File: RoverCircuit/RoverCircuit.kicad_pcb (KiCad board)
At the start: 2 copper layers, 92.2 x 67.7 mm, 57 parts, among them J11_Sample_IR_Diode1 JST_2Pin_P2.54_V, J12_Sat_Diode1 JST_2Pin_P2.54_V, J13_Laser1 JST_2Pin_P2.54_V, J14_QRD_Board1 JST_5Pin_P2.54_V, J15_Ball_QRD1 JST_3Pin_P2.54_V, J1_Servo1 JST_3Pin_P2.54_V, J2_Left_Wheel1 JST_4Pin_P2.54_V, J3_Right_Wheel1 JST_4Pin_P2.54_V, J4 JST_10Pin_P2.54_V, J5 JST_10Pin_P2.54_V, J6_Left_Sharp1 JST_3Pin_P2.54_V, J7_Right_Sharp1 JST_3Pin_P2.54_V, J8_Front_Sharp1 JST_3Pin_P2.54_V, J9_5v_Regulator1 JST_3Pin_P2.54_V, Q1 PMOS, Q2 NMOS, Q6 NMOS, U2 LM1117T-3.3, U3 LM324

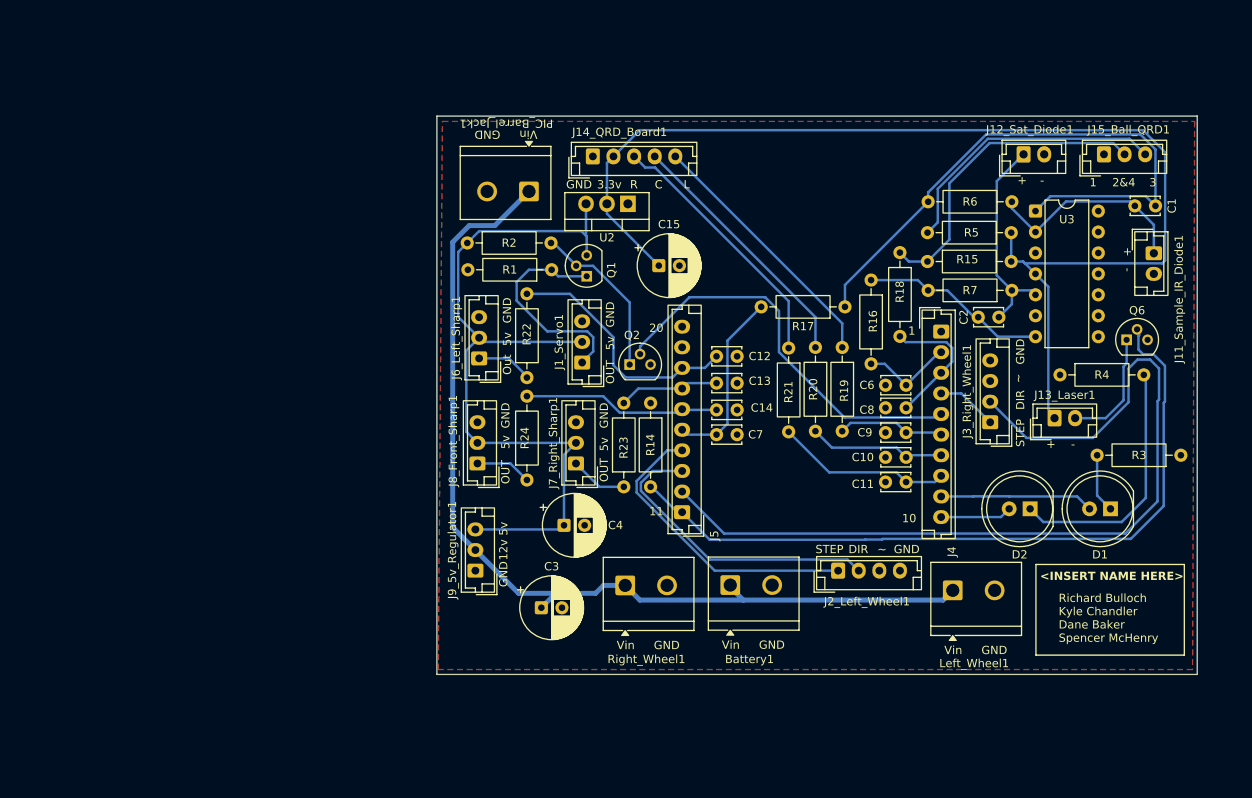
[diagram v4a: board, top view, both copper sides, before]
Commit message: Finalized circuit diagram, functional line following
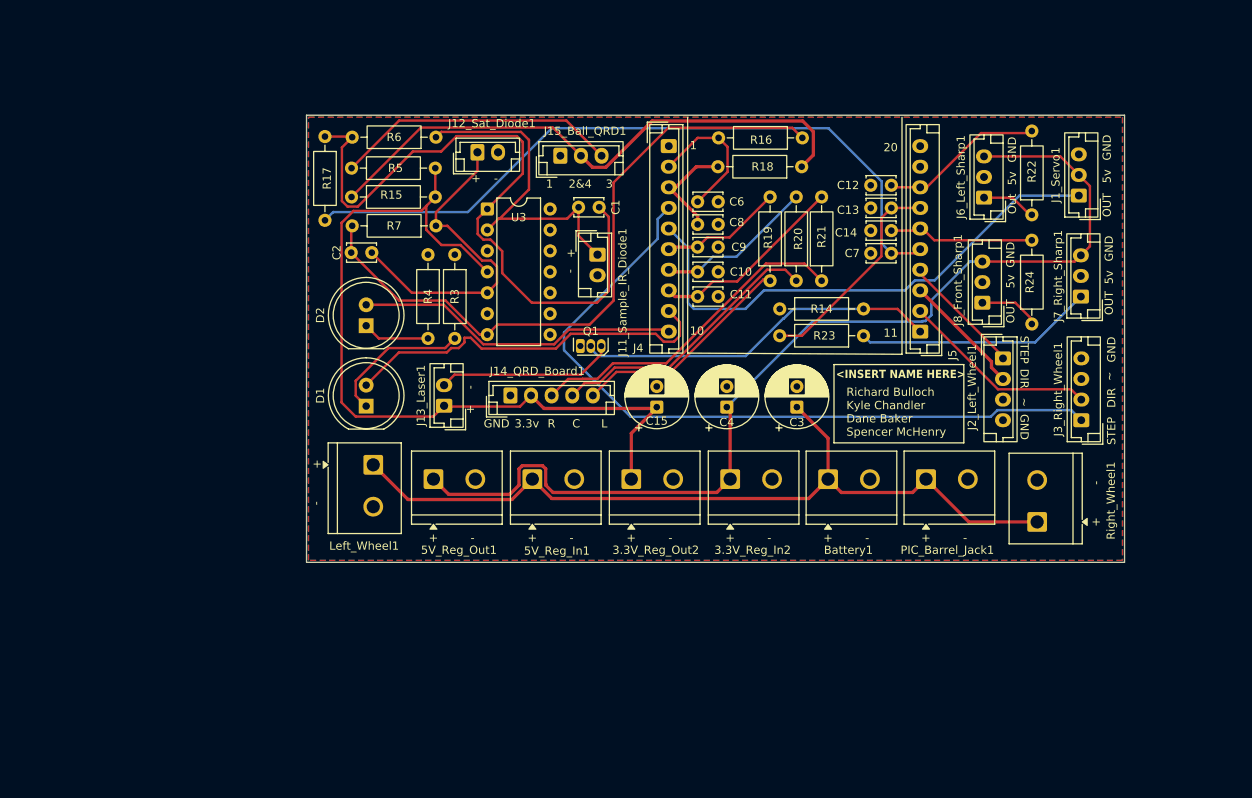
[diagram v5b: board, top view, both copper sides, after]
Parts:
- removed J9_5v_Regulator1: JST_3Pin_P2.54_V, Connector_JST:JST_EH_B3B-EH-A_1x03_P2.50mm_Vertical
- removed the Q1 at (120.5, 65.8)
- removed Q2: NMOS, Package_TO_SOT_THT:TO-92
- removed R1, R2: 10K, Resistor_THT:R_Axial_DIN0207_L6.3mm_D2.5mm_P10.16mm_Horizontal
- removed U2: LM1117T-3.3, Package_TO_SOT_THT:TO-220-3_Vertical
- added 3.3V_Reg_In2: Battery_Terminal, Custom_Library:screw_terminal, F.Cu at (140.6, 90.7)
- added 3.3V_Reg_Out2: Battery_Terminal, Custom_Library:screw_terminal, F.Cu at (128.6, 90.7)
- added 5V_Reg_In1: Battery_Terminal, Custom_Library:screw_terminal, F.Cu at (116.6, 90.7)
- added 5V_Reg_Out1: Battery_Terminal, Custom_Library:screw_terminal, F.Cu at (104.6, 90.7)
- Q1: renamed from Q6; value NMOS -> VN2106; footprint Package_TO_SOT_THT:TO-92 -> Package_TO_SOT_THT:TO-92S
- R16, R17, R18, R19, R20, R21, R22, R23, R24: value 150Ω -> 10kΩ
- R3, R4: value 330 -> 330Ω
- moved R3 91.4 mm to (104.5, 63.2), turned to -90 degrees
- moved D1 91.1 mm to (93.8, 81.5), turned to 90 degrees
- moved D2 83.5 mm to (93.8, 71.8), turned to 90 degrees
- moved R4 78.0 mm to (101.2, 63.2), turned to -90 degrees
- moved C2 76.5 mm to (94.4, 62.9)
- moved Left_Wheel1 74.5 mm to (94.3, 91.4), turned to -90 degrees
- moved J13_Laser1 74.1 mm to (103.2, 81.5), turned to 90 degrees
- moved R15 70.3 mm to (92.0, 56.2)
- moved R6 70.3 mm to (102.2, 48.9)
- moved R7 70.3 mm to (102.2, 59.7)
- moved R5 70.3 mm to (102.1, 52.7)
- moved J11_Sample_IR_Diode1 67.5 mm to (121.8, 63.2)
- moved C1 67.5 mm to (119.5, 57.4)
- moved U3 66.5 mm to (108.4, 57.6)
- moved R17 66.4 mm to (88.8, 48.8), turned to -90 degrees
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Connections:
- J1_Servo1 pad 1: Net-(J1_Servo1-Pin_1) -> /Servo_PWM
- J6_Left_Sharp1 pad 2: /5v_Rail -> GND
- J6_Left_Sharp1 pad 3: GND -> /5v_Rail
- J7_Right_Sharp1 pad 2: /5v_Rail -> GND
- J7_Right_Sharp1 pad 3: GND -> /5v_Rail
- J8_Front_Sharp1 pad 2: /5v_Rail -> GND
- J8_Front_Sharp1 pad 3: GND -> /5v_Rail
- Q1 pad 1: Net-(J13_Laser1-Pin_2) -> GND
- Q1 pad 3: GND -> Net-(J13_Laser1-Pin_2)
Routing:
- net /Right_Wheel_DIR: track 106.7 -> 24.0 mm
- net /Right_Wheel_Step: track 7.40 -> 89.5 mm
- net /Sample_Collection_IR_Input: track 22.2 -> 87.7 mm
- net /Satellite_IR_Output: track 22.8 -> 81.4 mm
- net /Laser_Output: track 90.1 -> 44.2 mm
- net /3.3v_Rail: track 141.3 -> 101.2 mm
- net /Ball_Color_QRD_Output: track 38.2 -> 69.2 mm
- net /5v_Rail: track 95.0 -> 125.9 mm
- net /Debug_LED_2: track 8.66 -> 39.5 mm
- net /Debug_LED_1: track 18.7 -> 46.3 mm
- net Net-(J1_Servo1-Pin_1): track 26.8 -> 0.00 mm
- net Net-(D2-K): track 30.8 -> 8.14 mm
- net /Left_Wheel_DIR: track 37.0 -> 14.9 mm
- net /Right_Sharp_Output: track 6.97 -> 29.0 mm
- net /Left_Wheel_Step: track 36.8 -> 14.9 mm
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- added copper zone on B.Cu, net GND
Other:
- board size 92.2 x 67.7 mm -> 99.2 x 54.2 mm
